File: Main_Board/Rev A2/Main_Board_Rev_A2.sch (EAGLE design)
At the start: 209 parts, among them J1 90814-0208, J12 22-27-2061-06, J15 1241050-5, J2 90814-0206, J3 90814-0208, J4 5504F1-09S-02A-03, J5 22-05-7048-04, J6 22-05-7048-04, J7 22-05-7058-05, J8 22-05-7048-04, J9 22-05-7028-02, K1 G6K-2G-Y, K2 G6K-2G-Y, K3 G6K-2G-Y, K4 G6K-2G-Y, P1 RB1-125BAG1A, SW1 B3FS-1050, SW2 B3FS-1050, T2 MMBT2222AL, U1 LT3686HDDPBF, U10 SN74LVC2G17DBVR, U11 MCP2561-E/SN, U12 TLV313, U2 TPL0401A, U3 SN74LVC3G17DCTR, U4 SN74LVC3G17DCTR, U5 LT3686HDDPBF, U6 LPC1768FBD100, U7 AT24C512C-SSHM-B, U8 SN74LVC3G17DCTR, U9 SN74LVC2G17DBVR, X1 ASE_50, X12 22-05-7038-03, X13 22-05-7038-03, X14 22-05-7038-03, X15 22-05-7038-03, X2 FC-135, X3 ASE-12, X4 MSTBA2, X5 22-05-7028-02, X6 USB3075-30-A, X7 3000, X8 22-05-7028-02

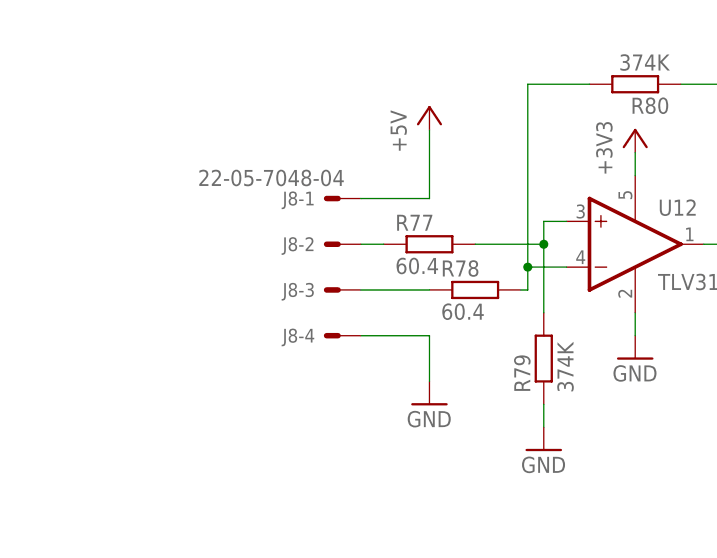
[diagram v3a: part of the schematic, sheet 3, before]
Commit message: Replace load pin connector into 5pts molex connector with GND MECA
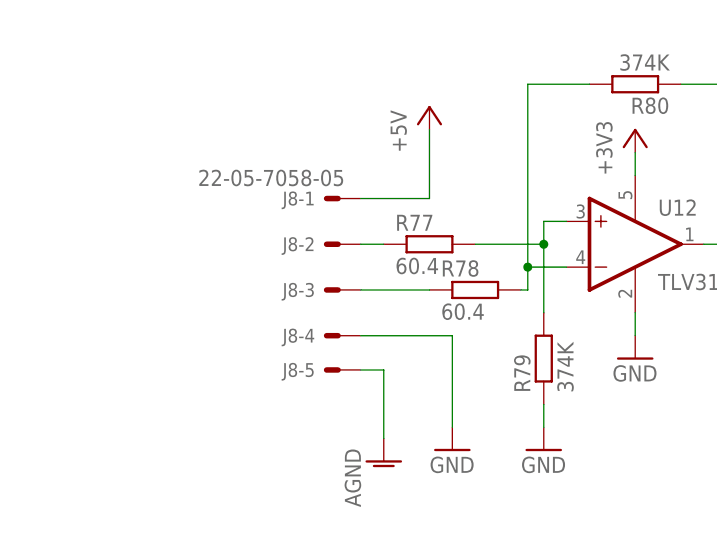
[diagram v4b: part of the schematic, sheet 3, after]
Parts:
- J8: value 22-05-7048-04 -> 22-05-7058-05; device con-molex:22-05-7048-04 -> con-molex:22-05-7058-05
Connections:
- net AGND: now also J8-5.S
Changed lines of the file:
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@@
 <attribute name="OC_NEWARK" value="86T3649"/>
 </part>
-<part name="J8" library="con-molex" deviceset="22-?-04" device="05-7048">
+<part name="J8" library="con-molex" deviceset="22-?-05" device="05-7058">
 <attribute name="MPN" value="22-05-7048"/>
 <attribute name="OC_NEWARK" value="26M6363"/>
@@
 <part name="GND88" library="supply1" deviceset="GND" device=""/>
 <part name="GND99" library="supply1" deviceset="GND" device=""/>
+<part name="AGND5" library="supply1" deviceset="AGND" device=""/>
 </parts>
 <sheets>
@@
 <instance part="J8" gate="-4" x="40.64" y="26.67" rot="MR0"/>
 <instance part="P+21" gate="1" x="50.8" y="52.07"/>
-<instance part="GND94" gate="1" x="50.8" y="19.05"/>
+<instance part="GND94" gate="1" x="53.34" y="13.97"/>
 <instance part="U12" gate="G$1" x="73.66" y="36.83">
 <attribute name="OC_NEWARK" x="73.66" y="36.83" size="1.778" layer="96" display="off"/>
@@
 <instance part="X12" gate="-3" x="40.64" y="137.16" rot="R180"/>
 <instance part="GND99" gate="1" x="45.72" y="124.46"/>
+<instance part="J8" gate="-5" x="40.64" y="22.86" rot="R180"/>
+<instance part="AGND5" gate="VR1" x="45.72" y="12.7"/>
 </instances>
 <busses>
@@
 <pinref part="J8" gate="-4" pin="S"/>
 <pinref part="GND94" gate="1" pin="GND"/>
-<wire x1="43.18" y1="26.67" x2="50.8" y2="26.67" width="0.1524" layer="91"/>
-<wire x1="50.8" y1="26.67" x2="50.8" y2="21.59" width="0.1524" layer="91"/>
+<wire x1="43.18" y1="26.67" x2="53.34" y2="26.67" width="0.1524" layer="91"/>
+<wire x1="53.34" y1="26.67" x2="53.34" y2="16.51" width="0.1524" layer="91"/>
 </segment>
 <segment>
@@
 </segment>
 </net>
+<net name="AGND" class="0">
+<segment>
+<pinref part="AGND5" gate="VR1" pin="AGND"/>
+<pinref part="J8" gate="-5" pin="S"/>
+<wire x1="45.72" y1="15.24" x2="45.72" y2="22.86" width="0.1524" layer="91"/>
+<wire x1="45.72" y1="22.86" x2="43.18" y2="22.86" width="0.1524" layer="91"/>
+</segment>
+</net>

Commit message: Generate MDP files
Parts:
- removed C102, C105, C129, C130, C131, C132, C133, C134: 0.1uF, rcl:C-EUC0603
- removed D3: MBRS140, diode:MBRS140
- removed GND: DP83848JSQ/NOPB, textas:DP83848JSQ/NOPB
- removed JP5: FIDUCIAL1X2, SparkFun:FIDUCIAL1X2
- removed P1: RB1-125BAG1A, con-wiznet:RB1-125BAG1A
- removed R108, R109, R110, R111: 100, rcl:R-EU_R0603
- removed X12, X13, X14, X15: 22-05-7038-03, con-molex:22-05-7038-03
- removed X7: 3000, keystone:3000
- removed X8: 22-05-7028-02, con-molex:22-05-7028-02
- added C46, C47, C50, C51: 2.2uF, rcl:C-EUC0603
- added C48, C49: 1000pF, rcl:C-EUC0603
- added C52, C53: 22uF, rcl:C-EUC0805
- added D1: MBRS140, diode:MBRS140
- added J10: 22-05-7048-04, con-molex:22-05-7048-04
- added J11: 22-05-7058-05, con-molex:22-05-7058-05
- added J14: 90814-0208, Molex_By_element14_Batch_1:90814-0208
- added J16: 90814-0206, Molex_By_element14_Batch_1:90814-0206
- added J17: MSTBA2, con-phoenix-508:MSTBA2
- added J18: 22-27-2061-06, con-molex:22-27-2061-06
- added J20: 1241050-5, con-amp:1241050-5
- added JP3: FIDUCIAL1X2, SparkFun:FIDUCIAL1X2
- added R15: 0R, rcl:R-EU_R0603
- added R60: 1K, rcl:R-EU_R0603
- added R66: 100, rcl:R-EU_R0603
- added R81: 1K5, rcl:R-EU_R0603
- added U13: LT3686HDDPBF, lineartechnology:LT3686HDDPBF
- C1: value 2.2uF -> 4.7uF; device rcl:C-EUC0603 -> rcl:CPOL-EUCT3216; MPN GRT188R61H225KE13D -> F931A475MAA; OC_NEWARK 01AC8938 -> 58R3271
- C10, C11: value 4.7uF -> 100nF; MPN MC0603X475K100CT -> MC0603B104K250CT; OC_NEWARK 06X6198 -> 06R4925
- C12: value 22uF -> 100nF; device rcl:C-EUC0805 -> rcl:C-EUC0603; MPN (none) -> MC0603B104K250CT; OC_NEWARK unknown -> 06R4925
- C16, C18, C20, C21, C22: value 100nF -> 0.1uF; MPN MC0603B104K250CT -> MC0603B104K160CT; OC_NEWARK 06R4925 -> 06R4923
- C17: value 10uF -> 0.1uF; device rcl:CPOL-EUCT3216 -> rcl:C-EUC0603; MPN F931A106MAA -> MC0603B104K160CT; OC_NEWARK 58R3260 -> 06R4923
- C19: value 100nF -> 18pF; MPN MC0603B104K250CT -> MC0603N180K500CT; OC_NEWARK 06R4925 -> 06R5140
- C2, C6: value 2.2uF -> 100nF; MPN GRT188R61H225KE13D -> MC0603B104K250CT; OC_NEWARK 01AC8938 -> 06R4925
- C23: value 4700pF -> 0.1uF; MPN MC0603B472K500CT -> MC0603B104K160CT; OC_NEWARK 33R0458 -> 06R4923
- C24: value 22uF -> 18pF; device rcl:C-EUC0805 -> rcl:C-EUC0603; MPN (none) -> MC0603N180K500CT; OC_NEWARK unknown -> 06R5140
- C26, C27: value 18pF -> 0.1uF; MPN MC0603N180K500CT -> MC0603B104K160CT; OC_NEWARK 06R5140 -> 06R4923
- C3: value 1000pF -> 100nF; MPN MC0603B102K500CT -> MC0603B104K250CT; OC_NEWARK 06R4910 -> 06R4925
- C35: value 10uF -> 4.7uF; device rcl:CPOL-EUCT3216 -> rcl:C-EUC0603; MPN F931A106MAA -> MC0603X475K100CT; OC_NEWARK 58R3260 -> 06X6198
- C36: value 0.1uF -> 4.7uF; MPN MC0603B104K160CT -> MC0603X475K100CT; OC_NEWARK 06R4923 -> 06X6198
- C4: value 1000pF -> 10uF; device rcl:C-EUC0603 -> rcl:CPOL-EUCT3216; MPN MC0603B102K500CT -> F931A106MAA; OC_NEWARK 06R4910 -> 58R3260
- C5: value 2.2uF -> 4700pF; MPN GRT188R61H225KE13D -> MC0603B472K500CT; OC_NEWARK 01AC8938 -> 33R0458
- C9: value 4.7uF -> 10uF; MPN F931A475MAA -> F931A106MAA; OC_NEWARK 58R3271 -> 58R3260
- J1: value 90814-0208 -> 22-05-7028-02; device Molex_By_element14_Batch_1:90814-0208 -> con-molex:22-05-7028-02
- J12: value 22-27-2061-06 -> 22-05-7028-02; device con-molex:22-27-2061-06 -> con-molex:22-05-7028-02; MF MOLEX -> (none); MPN 22-27-2061 -> 22-05-7028; OC_NEWARK 56H0719 -> 25M1728
- J15: value 1241050-5 -> 90814-0208; device con-amp:1241050-5 -> Molex_By_element14_Batch_1:90814-0208; MPN 1241050-5 -> (none); OC_NEWARK 98K5467 -> (none)
- J2: value 90814-0206 -> RB1-125BAG1A; device Molex_By_element14_Batch_1:90814-0206 -> con-wiznet:RB1-125BAG1A; OC_NEWARK (none) -> unknown
- J3: value 90814-0208 -> 5504F1-09S-02A-03; device Molex_By_element14_Batch_1:90814-0208 -> con-multicomp:5504F1-09S-02A-03; MPN (none) -> 5504F1-09S-02A-03; OC_NEWARK (none) -> 18T0703
- J4: value 5504F1-09S-02A-03 -> 22-05-7038-03; device con-multicomp:5504F1-09S-02A-03 -> con-molex:22-05-7038-03; MPN 5504F1-09S-02A-03 -> 22-05-7038; OC_NEWARK 18T0703 -> 26M6362
- J5: value 22-05-7048-04 -> 22-05-7038-03; device con-molex:22-05-7048-04 -> con-molex:22-05-7038-03; MPN 22-05-7048 -> 22-05-7038; OC_NEWARK 26M6363 -> 26M6362
- J6: value 22-05-7048-04 -> 22-05-7038-03; device con-molex:22-05-7048-04 -> con-molex:22-05-7038-03; MPN 22-05-7048 -> 22-05-7028; OC_NEWARK 26M6363 -> 25M1728
- J7: value 22-05-7058-05 -> 22-05-7038-03; device con-molex:22-05-7058-05 -> con-molex:22-05-7038-03; MF MOLEX -> (none); MPN 22-05-7058 -> 22-05-7028; OC_NEWARK 55H9619 -> 25M1728
- J9: value 22-05-7028-02 -> 22-05-7048-04; device con-molex:22-05-7028-02 -> con-molex:22-05-7048-04; MPN (none) -> 22-05-7048; OC_NEWARK (none) -> 26M6363
- L1: value 10uH -> 0603PS-103KLB; device Wurth-POWER_MAGNETICS-rev16f:WE-PD2_5848/5820 -> coilcraft:0603PS; MPN 74477410 -> (none); OC_NEWARK 08P2817 -> unknown
- L3: value 0603PS-103KLB -> 10uH; device coilcraft:0603PS -> Wurth-POWER_MAGNETICS-rev16f:WE-PD2_5848/5820; MPN (none) -> 74477410; OC_NEWARK unknown -> 08P2817
- LED1: value Red -> Blue; MPN OVS-0608 -> OVS-0603; OC_NEWARK 15R2208 -> 15R2205
- LED6: value Blue -> Red; MPN OVS-0603 -> OVS-0608; OC_NEWARK 15R2205 -> 15R2208
- R1: value 1K5 -> 220; MPN MCMR06X1501FTL -> MCMR06X2200FTL; OC_FARNELL 2073391 -> (none); OC_NEWARK 86T3542 -> 86T3577
- R10: value 1K -> 2K2; MPN MCMR06X1001FTL -> MCMR06X2201FTL; OC_NEWARK 86T3505 -> 86T3578
- R11: value 1K -> 10K; MPN MCMR06X1001FTL -> MCMR06X4701FTL; OC_NEWARK 86T3505 -> 86T3649
- R12, R13, R58, R9: value 1K -> 4K7; MPN MCMR06X1001FTL -> MCMR06X4701FTL; OC_NEWARK 86T3505 -> 86T3649
- R14: value 4K7 -> 0R; MPN MCMR06X4701FTL -> MCMR06X000 PTL; OC_NEWARK 86T3649 -> 86T3500
- R16: value 1K5 -> 10K; MPN MCMR06X1501FTL -> MCMR06X1002FTL; OC_FARNELL 2073391 -> (none); OC_NEWARK 86T3542 -> 86T3506
- R17: value 4K7 -> 10K; MPN MCMR06X4701FTL -> MCMR06X1002FTL; OC_NEWARK 86T3649 -> 86T3506
- R18, R19: value 220 -> 0R; MPN MCMR06X2200FTL -> MCMR06X000 PTL; OC_NEWARK 86T3577 -> 86T3500
- R2: value 4K7 -> 220; MPN MCMR06X4701FTL -> MCMR06X2200FTL; OC_NEWARK 86T3649 -> 86T3577
- R20: value 49.9 -> 1K5; MPN MCMR06X49R9FTL -> MCMR06X1501FTL; OC_NEWARK 86T3659 -> 86T3542
- R21, R22, R23: value 49.9 -> 100; MPN MCMR06X49R9FTL -> MCMR06X1000FTL; OC_NEWARK 86T3659 -> 86T3504
- R24: value 4K7 -> 100; MPN MCMR06X4701FTL -> MCMR06X1000FTL; OC_NEWARK 86T3649 -> 86T3504
- R25, R26: value 4K7 -> 60.4; MPN MCMR06X4701FTL -> MCMR06X1801FTL; OC_NEWARK 86T3649 -> 86T3556
- R27: value 4K7 -> 374K; MPN MCMR06X4701FTL -> MCMR06X1201FTL; OC_NEWARK 86T3649 -> 86T3525
- R28: value 2K2 -> 4K7; MPN MCMR06X2201FTL -> MCMR06X4701FTL; OC_NEWARK 86T3578 -> 86T3649
- R29: value 31K6 -> 4K7; MPN MC0603SAF3162T5E -> MCMR06X4701FTL; OC_FARNELL 2073391 -> (none); OC_NEWARK 79M5962 -> 86T3649
- R3: value 1K5 -> 49.9; MPN MCMR06X1501FTL -> MCMR06X49R9FTL; OC_NEWARK 86T3542 -> 86T3659
- R30: value 31K6 -> 374K; MPN MC0603SAF3162T5E -> MCMR06X1201FTL; OC_FARNELL 2073391 -> (none); OC_NEWARK 79M5962 -> 86T3525
- R31: value 10K -> 4K7; MPN MCMR06X1002FTL -> MCMR06X4701FTL; OC_FARNELL 2073391 -> (none); OC_NEWARK 86T3506 -> 86T3649
- R32: value 10K -> 4K7; MPN MCMR06X1002FTL -> MCMR06X4701FTL; OC_NEWARK 86T3506 -> 86T3649
- R33: value 52K3 -> 100; MPN MC0063W0603152K3 -> MCMR06X1000FTL; OC_FARNELL 2073391 -> (none); OC_NEWARK 26M0962 -> 86T3504
- R34, R37, R40: value 10K -> 100; MPN MCMR06X1002FTL -> MCMR06X1000FTL; OC_NEWARK 86T3506 -> 86T3504
- R35, R36: value 33 -> 1K5; MPN MCMR06X33R0FTL -> MCMR06X1501FTL; OC_NEWARK 86T3614 -> 86T3542
- R4, R5, R6: value 100 -> 49.9; MPN MCMR06X1000FTL -> MCMR06X49R9FTL; OC_NEWARK 86T3504 -> 86T3659
- R41, R47, R62: value 100 -> 1K; MPN MCMR06X1000FTL -> MCMR06X1001FTL; OC_NEWARK 86T3504 -> 86T3505
- R42, R46, R48: value 4K7 -> 1K; MPN MCMR06X4701FTL -> MCMR06X1001FTL; OC_NEWARK 86T3649 -> 86T3505
- R43, R45: value 100 -> 2K7; MPN MCMR06X1000FTL -> MCMR06X4701FTL; OC_NEWARK 86T3504 -> 86T3649
- R44: value 4K7 -> 2K7
- R49: OC_FARNELL 2073391 -> (none)
- R50, R51, R52: value 1K5 -> 10K; MPN MCMR06X1501FTL -> MCMR06X1002FTL; OC_NEWARK 86T3542 -> 86T3506
- R53: value 1K5 -> 100; MPN MCMR06X1501FTL -> MCMR06X1000FTL; OC_NEWARK 86T3542 -> 86T3504
- R54, R55: value 60.4 -> 100; MPN MCMR06X60R4FTL -> MCMR06X1000FTL; OC_NEWARK 86T3680 -> 86T3504
- R56: value 31K6 -> 100; MPN MC0603SAF3162T5E -> MCMR06X1000FTL; OC_FARNELL 2073391 -> (none); OC_NEWARK 79M5962 -> 86T3504
- R57: value 10K -> 4K7
- R61: value 100 -> 1K; MPN MCMR06X33R0FTL -> MCMR06X1001FTL; OC_NEWARK 86T3614 -> 86T3505
- R63, R64: value 10K -> 1K; MPN MCMR06X1002FTL -> MCMR06X1001FTL; OC_NEWARK 86T3506 -> 86T3505
- R65: value 0R -> 100; MPN MCMR06X000 PTL -> MCMR06X33R0FTL; OC_NEWARK 86T3500 -> 86T3614
- R67, R68: value 0R -> 31K6; MPN MCMR06X000 PTL -> MC0603SAF3162T5E; OC_FARNELL (none) -> 2073391; OC_NEWARK 86T3500 -> 79M5962
- R69: value 0R -> 4K7; MPN MCMR06X000 PTL -> MCMR06X4701FTL; OC_NEWARK 86T3500 -> 86T3649
- R7: value 100 -> 60.4; MPN MCMR06X1000FTL -> MCMR06X60R4FTL; OC_NEWARK 86T3504 -> 86T3680
- R70: value 1K5 -> 4K7; MPN MCMR06X1501FTL -> MCMR06X4701FTL; OC_NEWARK 86T3542 -> 86T3649
- R71: value 2K7 -> 52K3; MPN MCMR06X4701FTL -> MC0063W0603152K3; OC_FARNELL (none) -> 2073391; OC_NEWARK 86T3649 -> 26M0962
- R72, R74: value 1K -> 10K; MPN MCMR06X1001FTL -> MCMR06X1002FTL; OC_FARNELL (none) -> 2073391; OC_NEWARK 86T3505 -> 86T3506
- R73: value 2K7 -> 31K6; MPN MCMR06X4701FTL -> MC0603SAF3162T5E; OC_FARNELL (none) -> 2073391; OC_NEWARK 86T3649 -> 79M5962
- R75: value 1K -> 1K5; MPN MCMR06X1001FTL -> MCMR06X1501FTL; OC_FARNELL (none) -> 2073391; OC_NEWARK 86T3505 -> 86T3542
- R76: value 2K7 -> 1K5; MPN MCMR06X4701FTL -> MCMR06X1501FTL; OC_FARNELL (none) -> 2073391; OC_NEWARK 86T3649 -> 86T3542
- R77: value 60.4 -> 1K5; MPN MCMR06X1801FTL -> MCMR06X1501FTL; OC_NEWARK 86T3556 -> 86T3542
- R78: value 60.4 -> 33; MPN MCMR06X1801FTL -> MCMR06X33R0FTL; OC_NEWARK 86T3556 -> 86T3614
- R79: value 374K -> 33; MPN MCMR06X1201FTL -> MCMR06X33R0FTL; OC_NEWARK 86T3525 -> 86T3614
- R8: value 1K -> 60.4; MPN MCMR06X1001FTL -> MCMR06X60R4FTL; OC_NEWARK 86T3505 -> 86T3680
- R80: value 374K -> 1K5; MPN MCMR06X1201FTL -> MCMR06X1501FTL; OC_NEWARK 86T3525 -> 86T3542
- U1: value LT3686HDDPBF -> DP83848JSQ/NOPB; device lineartechnology:LT3686HDDPBF -> textas:DP83848JSQ/NOPB; MPN (none) -> DP83848JSQ/NOPB; OC_NEWARK (none) -> 96W2841
- U10, U9: value SN74LVC2G17DBVR -> SN74LVC3G17DCTR; device ti:SN74LVC2G17DBVR -> ti:SN74LVC3G17DCTR
- U11: value MCP2561-E/SN -> TPL0401A; device Microchip_By_element14_Batch_1:MCP2561-E/SN -> ti:TPL0401A; MPN MCP2561-E/SN -> ISL90727WIE627Z-T7A; OC_NEWARK 12X8698 -> 82Y6761
- U12: value TLV313 -> LT3686HDDPBF; device ti:TLV313 -> lineartechnology:LT3686HDDPBF; MPN TLV313IDBVT -> (none); OC_NEWARK 95Y0395 -> (none)
- U2: value TPL0401A -> MCP2561-E/SN; device ti:TPL0401A -> Microchip_By_element14_Batch_1:MCP2561-E/SN; MPN ISL90727WIE627Z-T7A -> MCP2561-E/SN; OC_NEWARK 82Y6761 -> 12X8698
- U3: value SN74LVC3G17DCTR -> AT24C512C-SSHM-B; device ti:SN74LVC3G17DCTR -> atmel:AT24C512C-SSHM-B; MF TEXAS INSTRUMENTS -> (none)
- U4: value SN74LVC3G17DCTR -> LPC1768FBD100; device ti:SN74LVC3G17DCTR -> NXP:LPC1768FBD100; MF TEXAS INSTRUMENTS -> (none); MPN (none) -> LPC1768FBD100; OC_NEWARK (none) -> 15R1840
- U5: value LT3686HDDPBF -> TLV313; device lineartechnology:LT3686HDDPBF -> ti:TLV313; MPN (none) -> TLV313IDBVT; OC_NEWARK (none) -> 95Y0395
- U6: value LPC1768FBD100 -> SN74LVC2G17DBVR; device NXP:LPC1768FBD100 -> ti:SN74LVC2G17DBVR; MF (none) -> TEXAS INSTRUMENTS; MPN LPC1768FBD100 -> (none); OC_NEWARK 15R1840 -> (none)
- U7: value AT24C512C-SSHM-B -> SN74LVC2G17DBVR; device atmel:AT24C512C-SSHM-B -> ti:SN74LVC2G17DBVR; MF (none) -> TEXAS INSTRUMENTS
- X4: value MSTBA2 -> 3000; device con-phoenix-508:MSTBA2 -> keystone:3000; MF (none) -> KEYSTONE ELECTR; MPN (none) -> 3000; OC_NEWARK (none) -> 66F5622
- renumbered C101 to C43, C103 to C39, C104 to C41, C106 to C40, C107 to C42, C108 to C44, C109 to C45, U$2 to T1, X5 to J13, X6 to J19
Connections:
- net !JTAG_TRST: now also J20.P$5, U4.*TRST; no longer J15.P$5, U6.*TRST
- net !RESET: now also R14.1, R16.1, U4.*RESET; no longer R63.1, R65.1, U6.*RESET
- net +24V: now also C46.1, C47.1, J10-1.S, J3C.9, J4-1.S, J7-1.S, J9-1.S, R69.2, R70.2, U12.EN/UVLO, U12.VIN, U13.EN/UVLO, U13.VIN; no longer C1.1, C2.1, J4C.9, R25.2, R26.2, U1.EN/UVLO, U1.VIN, U5.EN/UVLO, U5.VIN, X12-1.S, X13-1.S, X14-1.S, X15-1.S
- net +3V3: now also C1.+, C10.1, C11.1, C13.1, C16.1, C17.1, C2.1, C20.1, C21.1, C26.1, C27.1, C3.1, C53.1, J15.1, J16.1, J2.CT, J20.P$1, L1.1, L3.2, LED1.A, R10.1, R11.2, R12.2, R13.2, R16.2, R2.2, R4.1, R5.1, R57.1, R58.1, R6.1, R73.2, R76.2, R80.1, R81.1, U1.AVDD33, U1.IOVDD33, U1.IOVDD33_2, U13.BD, U4.NC, U4.VDD, U4.VDD_2, U4.VDD_3, U4.VDD_4, U4.VDD_5, U4.VDD_6, U5.V+, U6.VCC; no longer C129.1, C130.1, C14.1, C19.1, C29.1, C30.1, C31.1, C35.+, C36.1, C37.1, C38.1, C7.1, C8.1, GND.AVDD33, GND.IOVDD33, GND.IOVDD33_2, J15.P$1, J2.1, J3.1, L1.2, L3.1, LED5.A, P1.CT, R14.1, R18.2, R19.2, R2.1, R20.1, R21.1, R22.1, R23.1, R27.2, R28.1, R38.1, R56.2, R57.2, R63.2, R64.2, U1.BD, U12.V+, U4.VCC, U6.NC, U6.VDD, U6.VDD_2, U6.VDD_3, U6.VDD_4, U6.VDD_5, U6.VDD_6
- net +5V: now also C14.1, C52.1, J1-1.S, J11-4.S, J14.4, R28.1, R29.1, R31.1, R32.1, R35.2, R36.2, R38.2, R39.2, R43.1, R45.1, R65.1, R71.2, R75.2, U11.H, U12.BD; no longer C13.1, C24.1, J1.4, J7-4.S, J9-1.S, R16.2, R33.2, R42.1, R46.1, R48.1, R50.2, R51.2, R52.2, R53.2, R61.1, R71.1, R73.1, R76.1, U2.H, U5.BD
- net ADC_SLACK_DETECTION: now also R30.1, U4.P0[23]/AD0[0]/I2SRX_CLK/CAP3[0], U5.OUT; no longer R80.1, U12.OUT, U6.P0[23]/AD0[0]/I2SRX_CLK/CAP3[0]
- net ADC_TEMP_0: now also C35.1, R51.1, U4.P0[25]/AD0[2]/I2SRX_SDA/TXD3; no longer C11.1, R40.1, U6.P0[25]/AD0[2]/I2SRX_SDA/TXD3
- net ADC_TEMP_1: now also C36.1, R52.2, U4.P0[24]/AD0[1]/I2SRX_WS/CAP3[1]; no longer C10.1, R34.2, U6.P0[24]/AD0[1]/I2SRX_WS/CAP3[1]
- net AGND: now also J2.P$1, J3S.SHIELD; no longer J4S.SHIELD, P1.P$1
- net AVDD: now also C23.1, J12-1.S, L1.2, U4.VDDA, U4.VREFP; no longer C28.1, L3.2, U6.VDDA, U6.VREFP, X8-1.S
- net BOOT_SELECT_P2_10: now also R18.1, U4.P2[10]/*EINT0/NMI; no longer R68.1, U6.P2[10]/*EINT0/NMI
- net BOOT_SELECT_P2_12: now also R19.1, U4.P2[12]/*EINT2/I2STX_WS; no longer R69.1, U6.P2[12]/*EINT2/I2STX_WS
- net BRAKE_SENSOR_1: now also U4.P1[22]/MCOB0/USB_PWRD/MAT1[0], U6.1Y; no longer U10.1Y, U6.P1[22]/MCOB0/USB_PWRD/MAT1[0]
- net BRAKE_SENSOR_2: now also U4.P1[25]/MCOA1/MAT1[1], U6.2Y; no longer U10.2Y, U6.P1[25]/MCOA1/MAT1[1]
- net CAN_N: now also J3C.2, R7.1, U2.CANL; no longer J4C.2, R55.1, U11.CANL
- net CAN_P: now also J3C.7, R8.2, U2.CANH; no longer J4C.7, R54.2, U11.CANH
- net CAN_SHLD: now also J3C.5; no longer J4C.5
- net CAN_SPLIT: now also C5.2, U2.SPLIT; no longer C23.2, U11.SPLIT
- net CAN_X_N: now also U2.RXD, U4.P0[0]/RD1/TXD3/SDA1; no longer U11.RXD, U6.P0[0]/RD1/TXD3/SDA1
- net CAN_X_P: now also U2.TXD, U4.P0[1]/TD1/RXD3/SCL1; no longer U11.TXD, U6.P0[1]/TD1/RXD3/SCL1
- net DRIVE_EN: now also U4.P1[26]/MCOB1/PWM1[6]/CAP0[0], U7.1Y; no longer U6.P1[26]/MCOB1/PWM1[6]/CAP0[0], U9.1Y
- net DRIVE_ERR: now also U4.P1[29]/MCOB2/PCAP1[1]/MAT0[1], U7.2Y; no longer U6.P1[29]/MCOB2/PCAP1[1]/MAT0[1], U9.2Y
- net EEPROM_SCL: now also R13.1, U3.SCL, U4.P0[28]/SCL0/USB_SCL; no longer R27.1, U6.P0[28]/SCL0/USB_SCL, U7.SCL
- net EEPROM_SDA: now also R12.1, U3.SDA, U4.P0[27]/SDA0/USB_SDA; no longer R17.1, U6.P0[27]/SDA0/USB_SDA, U7.SDA
- net ENCODER_A: now also U4.P1[20]/MCI0/PWM1[2]/SCK0; no longer U6.P1[20]/MCI0/PWM1[2]/SCK0
- net ENCODER_B: now also U4.P1[23]/MCI1/PWM1[4]/MISO0; no longer U6.P1[23]/MCI1/PWM1[4]/MISO0
- net ENCODER_Z: now also U4.P1[24]/MCI2/PWM1[5]/MOSI0; no longer U6.P1[24]/MCI2/PWM1[5]/MOSI0
- net ETH_CLK_EN: now also U4.P1[27]/CLKOUT/*USB_OVRCR/CAP0[1]; no longer U6.P1[27]/CLKOUT/*USB_OVRCR/CAP0[1]
- net ETH_CRS: now also U1.CRS/CRS_DV/LED_CFG, U4.P1[8]/ENET_CRS; no longer GND.CRS/CRS_DV/LED_CFG, U6.P1[8]/ENET_CRS
- net ETH_MDC: now also U1.MDC, U4.P1[16]/ENET_MDC; no longer GND.MDC, U6.P1[16]/ENET_MDC
- net ETH_MDIO: now also U1.MDIO, U4.P1[17]/ENET_MDIO; no longer GND.MDIO, U6.P1[17]/ENET_MDIO
- net ETH_RST: now also U1.RESET_N, U4.P1[28]/MCOA2/PCAP1[0]/MAT0[0]; no longer GND.RESET_N, U6.P1[28]/MCOA2/PCAP1[0]/MAT0[0]
- net ETH_RXD_0: now also U1.RXD_0/PHYAD1, U4.P1[9]/ENET_RXD0; no longer GND.RXD_0/PHYAD1, U6.P1[9]/ENET_RXD0
- net ETH_RXD_1: now also U1.RXD_1/PHYAD2, U4.P1[10]/ENET_RXD1; no longer GND.RXD_1/PHYAD2, U6.P1[10]/ENET_RXD1
- net ETH_RX_ER: now also U1.RX_ER/MDIX_EN, U4.P1[14]/ENET_RX_ER; no longer GND.RX_ER/MDIX_EN, U6.P1[14]/ENET_RX_ER
- net ETH_RX_N: now also J2.RD-, R6.2, U1.RD-; no longer GND.RD-, P1.RD-, R23.2
- net ETH_RX_P: now also J2.RD+, R5.2, U1.RD+; no longer GND.RD+, P1.RD+, R22.2
- net ETH_TXD_0: now also U1.TXD_0, U4.P1[0]/ENET_TXD0; no longer GND.TXD_0, U6.P1[0]/ENET_TXD0
- net ETH_TXD_1: now also U1.TXD_1, U4.P1[1]/ENET_TXD1; no longer GND.TXD_1, U6.P1[1]/ENET_TXD1
- net ETH_TXD_EN: now also U1.TX_EN, U4.P1[4]/ENET_TX_EN; no longer GND.TX_EN, U6.P1[4]/ENET_TX_EN
- net ETH_TX_N: now also J2.TD-, R4.2, U1.TD-; no longer GND.TD-, P1.TD-, R21.2
- net ETH_TX_P: now also J2.TD+, R3.2, U1.TD+; no longer GND.TD+, P1.TD+, R20.2
- net ETH_X1: now also U1.X1, U4.P1[15]/ENET_REF_CLK; no longer GND.X1, U6.P1[15]/ENET_REF_CLK
- net FAN_1_PWM: now also R41.2, U4.P3[25]/MAT0[0]/PWM1[2]; no longer R58.2, U6.P3[25]/MAT0[0]/PWM1[2]
- net FAN_2_PWM: now also R42.2, U4.P3[26]/STCLK/MAT0[1]/PWM1[3]; no longer R59.2, U6.P3[26]/STCLK/MAT0[1]/PWM1[3]
- net GND: now also C1.-, C17.2, C23.2, C35.2, C4.-, C46.2, C47.2, C48.2, C49.2, C52.2, C53.2, C6.2, J1-2.S, J10-4.S, J11-1.S, J14.2, J14.3, J15.8, J16.6, J17-2.1, J18-1.S, J2.R4, J2.R5, J2.R6, J20.P$2, J3C.3, J3C.6, J4-3.S, J5-3.S, J6-3.S, J7-3.S, J9-4.S, LED7.C, LED8.C, LED9.C, R27.1, R50.2, R67.1, R68.1, R72.1, R74.1, R9.2, U1.AGND, U1.AGND_2, U1.DAP, U1.DGND, U1.IOGND, U11.GND, U12.EP, U12.MODE, U13.EP, U13.MODE, U2.STBY, U2.VSS, U3.A0, U3.A1, U3.A2, U4.VREFN, U4.VSS, U4.VSSA, U4.VSS_2, U4.VSS_3, U4.VSS_4, U4.VSS_5, U4.VSS_6, U5.V-, U6.GND, X4.VBAT-; no longer C1.2, C102.2, C105.2, C129.2, C130.2, C131.2, C132.2, C133.2, C134.2, C17.-, C35.-, C4.2, GND.AGND, GND.AGND_2, GND.DAP, GND.DGND, GND.IOGND, J1.2, J1.3, J12-1.S, J15.P$2, J2.6, J3.8, J4C.3, J4C.6, J5-4.S, J6-4.S, J7-1.S, J9-2.S, LED2.C, LED3.C, LED4.C, P1.R4, P1.R5, P1.R6, R24.2, R29.1, R30.1, R31.1, R32.2, R37.1, R79.1, U1.EP, U1.MODE, U11.STBY, U11.VSS, U12.V-, U2.GND, U4.GND, U5.EP, U5.MODE, U6.VREFN, U6.VSS, U6.VSSA, U6.VSS_2, U6.VSS_3, U6.VSS_4, U6.VSS_5, U6.VSS_6, U7.A0, U7.A1, U7.A2, X12-3.S, X13-3.S, X14-3.S, X15-3.S, X4-2.1, X7.VBAT-
- net HMI_BUTTON_1: now also J15.2, R59.1; no longer J3.2, R13.1
- net HMI_BUTTON_2: now also J15.3, R60.1; no longer J3.3, R12.1
- net HMI_BUTTON_3: now also J15.4, R61.1; no longer J3.4, R11.1
- net HMI_BUTTON_4: now also J15.5, R62.1; no longer J3.5, R10.1
- net HMI_BUTTON_5: now also J15.6, R63.1; no longer J3.6, R9.1
- net HMI_BUTTON_6: now also J15.7, R64.1; no longer J3.7, R8.1
- net HMI_BUTTON_ISO_1: now also U4.P0[16]/RXD1/SSEL0/SSEL, U9.1Y; no longer U4.1Y, U6.P0[16]/RXD1/SSEL0/SSEL
- net HMI_BUTTON_ISO_2: now also U4.P0[15]/TXD1/SCK0/SCK, U9.2Y; no longer U4.2Y, U6.P0[15]/TXD1/SCK0/SCK
- net HMI_BUTTON_ISO_3: now also U4.P0[17]/CTS1/MISO0/MISO, U9.3Y; no longer U4.3Y, U6.P0[17]/CTS1/MISO0/MISO
- net HMI_BUTTON_ISO_4: now also U10.1Y, U4.P0[18]/DCD1/MOSI0/MOSI; no longer U3.1Y, U6.P0[18]/DCD1/MOSI0/MOSI
- net HMI_BUTTON_ISO_5: now also U10.2Y, U4.P0[19]/DSR1/SDA1; no longer U3.2Y, U6.P0[19]/DSR1/SDA1
- net HMI_BUTTON_ISO_6: now also R14.2, R15.1, U10.3Y; no longer R65.2, R67.1, U3.3Y
- net HMI_BUTTON_MCU_FCT_6: now also R15.2, U4.P0[20]/DTR1/SCL1; no longer R67.2, U6.P0[20]/DTR1/SCL1
- net HMI_LCD_BACKLIGHT: now also R66.2, U4.P0[22]/RTS1/TD1; no longer R62.2, U6.P0[22]/RTS1/TD1
- net HMI_LCD_LED+: now also J14.1, R65.2; no longer J1.1, R61.2
- net HMI_LCD_SCL: now also J14.6, R57.2, U11.SCL, U4.P0[11]/RXD2/SCL2/MAT3[1]; no longer J1.6, R14.2, U2.SCL, U6.P0[11]/RXD2/SCL2/MAT3[1]
- net HMI_LCD_SDA: now also J14.5, R58.2, U11.SDA, U4.P0[10]/TXD2/SDA2/MAT3[0]; no longer J1.5, R2.2, U2.SDA, U6.P0[10]/TXD2/SDA2/MAT3[0]
- net HMI_LCD_VO: now also J14.7, U11.W; no longer J1.7, U2.W
- net HMI_LED_1: now also R55.1, U4.P2[2]/PWM1[3]/CTS1/TRACEDATA[3]; no longer R7.1, U6.P2[2]/PWM1[3]/CTS1/TRACEDATA[3]
- net HMI_LED_2: now also R53.2, U4.P2[3]/PWM1[4]/DCD1/TRACEDATA[2]; no longer R6.2, U6.P2[3]/PWM1[4]/DCD1/TRACEDATA[2]
- net HMI_LED_3: now also R56.1, U4.P2[4]/PWM1[5]/DSR1/TRACEDATA[1]; no longer R5.1, U6.P2[4]/PWM1[5]/DSR1/TRACEDATA[1]
- net HMI_LED_4: now also R54.2, U4.P2[5]/PWM1[6]/DTR1/TRACEDATA[0]; no longer R4.2, U6.P2[5]/PWM1[6]/DTR1/TRACEDATA[0]
- net ISP_RXDO: now also J18-4.S, J20.P$3, U4.P0[3]/RXD0/AD0[6]; no longer J12-4.S, J15.P$3, U6.P0[3]/RXD0/AD0[6]
- net ISP_TXDO: now also J18-5.S, J20.P$4, U4.P0[2]/TXD0/AD0[7]; no longer J12-5.S, J15.P$4, U6.P0[2]/TXD0/AD0[7]
- net JTAG_TCK: now also J20.P$8, U4.TCK/SWDCLK; no longer J15.P$8, U6.TCK/SWDCLK
- net JTAG_TDI: now also J20.P$7, U4.TDI; no longer J15.P$7, U6.TDI
- net JTAG_TDO: now also J20.P$9, U4.TDO/SWO; no longer J15.P$9, U6.TDO/SWO
- net JTAG_TMS: now also J20.P$10, U4.TMS/SWDIO; no longer J15.P$10, U6.TMS/SWDIO
- net L1_1: now also J2.L2, U1.LED_LINK/AN0; no longer GND.LED_LINK/AN0, P1.L2
- net L1_2: now also J2.L4, U1.LED_SPEED/AN1; no longer GND.LED_SPEED/AN1, P1.L4
- net LED_DEBUG: now also R20.2, U4.P0[9]/I2STX_SDA/MOSI1/MAT2[3]; no longer R70.2, U6.P0[9]/I2STX_SDA/MOSI1/MAT2[3]
- net MII_MODE: now also R10.2, U1.RX_DV/MII_MODE; no longer GND.RX_DV/MII_MODE, R28.2
- net N$1: now also J16.3, R53.1; no longer J2.3, R6.1
- net N$10: now also R68.2, U13.RT; no longer R30.2, U1.RT
- net N$11: now also J9-2.S, R41.1; no longer J5-2.S, R58.1
- net N$12: now also J11-3.S, R43.2, R46.1; no longer J7-3.S, R71.2, R72.1
- net N$13: now also J10-2.S, R42.1; no longer J6-2.S, R59.1
- net N$14: now also J11-5.S, R44.2, R47.1; no longer J7-5.S, R74.1, R76.2
- net N$15: now also R78.1, R81.2; no longer R3.2, R36.1
- net N$16: now also R79.1, R80.2; no longer R35.1, R38.2
- net N$17: now also C37.1, R59.2, U9.1A; no longer C102.1, R13.2, U4.1A
- net N$18: now also LED10.C, R77.1; no longer LED5.C, R39.1
- net N$19: now also R60.2, U9.2A; no longer R12.2, U4.2A
- net N$2: now also J16.5, R54.1; no longer J2.5, R4.1
- net N$20: now also R61.2, U9.3A; no longer R11.2, U4.3A
- net N$21: now also J4-2.S, R21.1; no longer R109.1, X14-2.S
- net N$22: now also C49.1, U13.SS; no longer C4.1, U1.SS
- net N$23: now also J5-2.S, R22.1; no longer R108.1, X15-2.S
- net N$24: now also K11.+, R21.2; no longer K31.+, R109.2
- net N$25: now also C38.1, R62.2, U10.1A; no longer C105.1, R10.2, U3.1A
- net N$26: now also R63.2, U10.2A; no longer R9.2, U3.2A
- net N$27: now also R64.2, U10.3A; no longer R8.2, U3.3A
- net N$28: now also K31.+, R23.2; no longer K11.+, R111.2
- net N$3: now also C5.1, R7.2, R8.1; no longer C23.1, R54.1, R55.2
- net N$30: now also R71.1, R72.2, U12.FB; no longer R31.2, R33.1, U5.FB
- net N$31: now also C50.1, U12.BOOST; no longer C5.1, U5.BOOST
- net N$32: now also J6-2.S, R23.1; no longer R111.1, X12-2.S
- net N$33: now also K41.+, R24.2; no longer K21.+, R110.2
- net N$34: now also C50.2, D1.C, U12.SW; no longer C5.2, D2.C, U5.SW
- net N$35: now also D1.A, U12.DA; no longer D2.A, U5.DA
- net N$36: now also R73.1, R74.2, U13.FB; no longer R49.2, R56.1, U1.FB
- net N$37: now also J7-2.S, R24.1; no longer R110.1, X13-2.S
- net N$38: now also C29.1, R34.2, U6.2A; no longer C131.1, R47.2, U10.2A
- net N$39: now also C28.1, R33.2, U6.1A; no longer C132.1, R45.2, U10.1A
- net N$4: now also R9.1, U1.RBIAS; no longer GND.RBIAS, R24.1
- net N$40: now also C51.1, U13.BOOST; no longer C6.1, U1.BOOST
- net N$41: now also C30.1, R37.2, U7.1A; no longer C134.1, R41.2, U9.1A
- net N$42: now also C31.1, R40.2, U7.2A; no longer C133.1, R43.2, U9.2A
- net N$43: now also C51.2, D2.C, L3.1, U13.SW; no longer C6.2, D3.C, L1.1, U1.SW
- net N$44: now also LED7.A, R70.1; no longer LED2.A, R26.1
- net N$45: now also LED6.C, R69.1; no longer LED1.C, R25.1
- net N$46: now also D2.A, U13.DA; no longer D3.A, U1.DA
- net N$47: now also R11.1, U3.WP; no longer R57.1, U7.WP
- net N$48: now also R17.1, R18.2, R19.2; no longer R64.1, R68.2, R69.2
- net N$49: now also LED1.C, R20.1; no longer LED10.C, R70.1
- net N$5: now also R67.2, U12.RT; no longer R29.2, U5.RT
- net N$50: now also LED9.A, R76.1; no longer LED4.A, R1.1
- net N$51: now also LED8.A, R75.1; no longer LED3.A, R16.1
- net N$52: now also J11-2.S, R45.2, R48.1; no longer J7-2.S, R73.2, R75.1
- net N$53: now also R48.2; no longer R75.2
- net N$54: now also R47.2; no longer R74.2
- net N$55: now also K21.+, R22.2; no longer K41.+, R108.2
- net N$58: now also K13.S, LED2.C, R28.2, R33.1; no longer K33.S, LED8.C, R45.1, R46.2
- net N$6: now also C48.1, U12.SS; no longer C3.1, U5.SS
- net N$61: now also R46.2; no longer R72.2
- net N$62: now also R25.1; no longer R77.1
- net N$63: now also J16.2, R55.2; no longer J2.2, R7.2
- net N$64: now also J16.4, R56.2; no longer J2.4, R5.2
- net N$65: now also J12-2.S, R49.2, R51.2; no longer R37.2, R40.2, X8-2.S
- net N$66: now also R50.1, R52.1; no longer R32.1, R34.1
- net N$67: now also R66.1; no longer R62.1
- net N$70: now also LED2.A, R35.1; no longer LED8.A, R52.1
- net N$71: now also K23.S, LED3.C, R29.2, R34.1; no longer K43.S, LED9.C, R47.1, R48.2
- net N$72: now also LED3.A, R36.1; no longer LED9.A, R53.1
- net N$73: now also K33.S, LED4.C, R31.2, R37.1; no longer K13.S, LED6.C, R41.1, R42.2
- net N$74: now also LED4.A, R38.1; no longer LED6.A, R50.1
- net N$75: now also K43.S, LED5.C, R32.2, R40.1; no longer K23.S, LED7.C, R43.1, R44.2
- net N$76: now also LED5.A, R39.1; no longer LED7.A, R51.1
- net N$78: now also R26.1; no longer R78.1
- net N$79: now also R25.2, R27.2, U5.+IN; no longer R77.2, R79.2, U12.+IN
- net N$8: now also J2.L1, R1.1; no longer P1.L1, R19.1
- net N$80: now also R26.2, R30.2, U5.-IN; no longer R78.2, R80.2, U12.-IN
- net N$9: now also J2.L3, R2.1; no longer P1.L3, R18.1
- net PFBOUT: now also C4.+, C6.1, C7.1, C8.1, U1.PFBIN1, U1.PFBIN2, U1.PFBOUT; no longer C16.1, C17.+, C20.1, C21.1, GND.PFBIN1, GND.PFBIN2, GND.PFBOUT
- net RTCX1: now also C19.1, U4.RTCX1; no longer C26.1, U6.RTCX1
- net RTCX2: now also C24.1, U4.RTCX2; no longer C27.1, U6.RTCX2
- net USB_D_N: now also R78.2, U4.P0[30]/USB_D?; no longer R36.2, U6.P0[30]/USB_D?
- net USB_D_P: now also R79.2, U4.P0[29]/USB_D+; no longer R35.2, U6.P0[29]/USB_D+
- net USB_UP_LED: now also R77.2, U4.P1[18]/USB_UP_LED/PWM1[1]/CAP1[0]; no longer R39.2, U6.P1[18]/USB_UP_LED/PWM1[1]/CAP1[0]
- net USB_V_BUS: now also U4.P1[30]/VBUS/AD0[4]; no longer U6.P1[30]/VBUS/AD0[4]
- net VBAT+: now also U4.VBAT, X4.VBAT+; no longer U6.VBAT, X7.VBAT+
- net VIN: now also J17-1.1, LED6.A; no longer LED1.A, X4-1.1
- net XTAL1: now also U4.XTAL1; no longer U6.XTAL1

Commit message: Update component reference
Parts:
- J1: MPN (none) -> 22-05-7028; OC_NEWARK (none) -> 25M1728
- J6, J7: MPN 22-05-7028 -> 22-05-7038; OC_NEWARK 25M1728 -> 26M6362
- J8: MF (none) -> MOLEX; MPN 22-05-7048 -> 22-05-7058; OC_NEWARK 26M6363 -> 55H9619
- R11: MPN MCMR06X4701FTL -> MCMR06X1002FTL; OC_NEWARK 86T3649 -> 86T3506
- R25, R26: MPN MCMR06X1801FTL -> MCMR06X60R4FTL; OC_NEWARK 86T3556 -> 86T3680
- R27, R30: MPN MCMR06X1201FTL -> CRCW0603374KFKEA.; OC_NEWARK 86T3525 -> 27W4235
- R43, R44, R45: MPN MCMR06X4701FTL -> MCMR06X2701FTL; OC_NEWARK 86T3649 -> 86T3598
- R65: MPN MCMR06X33R0FTL -> MCMR06X1000FTL; OC_NEWARK 86T3614 -> 86T3504
- T2: MPN (none) -> MMBT2222ALT3G; OC_NEWARK (none) -> 10N9478
- TP3, TP6: OC_NEWARK (none) -> unknown
- U3: MPN (none) -> AT24C512C-SSHM-B; OC_NEWARK (none) -> 68T4128
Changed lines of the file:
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@@
 </part>
 <part name="J6" library="con-molex" deviceset="22-?-03" device="05-7038">
-<attribute name="MPN" value="22-05-7028"/>
-<attribute name="OC_NEWARK" value="25M1728"/>
+<attribute name="MPN" value="22-05-7038"/>
+<attribute name="OC_NEWARK" value="26M6362"/>
 </part>
 <part name="P+12" library="supply1" deviceset="+5V" device=""/>
@@
 </part>
 <part name="J7" library="con-molex" deviceset="22-?-03" device="05-7038">
-<attribute name="MPN" value="22-05-7028"/>
-<attribute name="OC_NEWARK" value="25M1728"/>
+<attribute name="MPN" value="22-05-7038"/>
+<attribute name="OC_NEWARK" value="26M6362"/>
 </part>
 <part name="P+13" library="supply1" deviceset="+5V" device=""/>
@@
 <part name="U3" library="atmel" deviceset="AT24C512C-SSHM-B" device="">
 <attribute name="MF" value=""/>
+<attribute name="MPN" value="AT24C512C-SSHM-B"/>
+<attribute name="OC_NEWARK" value="68T4128"/>
 </part>
 <part name="+3V315" library="supply1" deviceset="+3V3" device=""/>
@@
 <part name="R11" library="rcl" deviceset="R-EU_" device="R0603" value="10K">
 <attribute name="MF" value=""/>
-<attribute name="MPN" value="MCMR06X4701FTL"/>
-<attribute name="OC_NEWARK" value="86T3649"/>
+<attribute name="MPN" value="MCMR06X1002FTL"/>
+<attribute name="OC_NEWARK" value="86T3506"/>
 </part>
 <part name="X3" library="crystal" deviceset="ASE" device="" value="ASE-12">
@@
 <part name="R43" library="rcl" deviceset="R-EU_" device="R0603" value="2K7">
 <attribute name="MF" value=""/>
-<attribute name="MPN" value="MCMR06X4701FTL"/>
-<attribute name="OC_NEWARK" value="86T3649"/>
+<attribute name="MPN" value="MCMR06X2701FTL"/>
+<attribute name="OC_NEWARK" value="86T3598"/>
 </part>
 <part name="R46" library="rcl" deviceset="R-EU_" device="R0603" value="1K">
@@
 <part name="R45" library="rcl" deviceset="R-EU_" device="R0603" value="2K7">
 <attribute name="MF" value=""/>
-<attribute name="MPN" value="MCMR06X4701FTL"/>
-<attribute name="OC_NEWARK" value="86T3649"/>
+<attribute name="MPN" value="MCMR06X2701FTL"/>
+<attribute name="OC_NEWARK" value="86T3598"/>
 </part>
 <part name="R47" library="rcl" deviceset="R-EU_" device="R0603" value="1K">
@@
 <part name="R44" library="rcl" deviceset="R-EU_" device="R0603" value="2K7">
 <attribute name="MF" value=""/>
-<attribute name="MPN" value="MCMR06X4701FTL"/>
-<attribute name="OC_NEWARK" value="86T3649"/>
+<attribute name="MPN" value="MCMR06X2701FTL"/>
+<attribute name="OC_NEWARK" value="86T3598"/>
 </part>
 <part name="J8" library="con-molex" deviceset="22-?-05" device="05-7058">
-<attribute name="MPN" value="22-05-7048"/>
-<attribute name="OC_NEWARK" value="26M6363"/>
+<attribute name="MF" value="MOLEX"/>
+<attribute name="MPN" value="22-05-7058"/>
+<attribute name="OC_NEWARK" value="55H9619"/>
 </part>
 <part name="P+9" library="supply1" deviceset="+5V" device=""/>
@@
 <part name="R25" library="rcl" deviceset="R-EU_" device="R0603" value="60.4">
 <attribute name="MF" value=""/>
-<attribute name="MPN" value="MCMR06X1801FTL"/>
-<attribute name="OC_NEWARK" value="86T3556"/>
+<attribute name="MPN" value="MCMR06X60R4FTL"/>
+<attribute name="OC_NEWARK" value="86T3680"/>
 </part>
 <part name="R26" library="rcl" deviceset="R-EU_" device="R0603" value="60.4">
 <attribute name="MF" value=""/>
-<attribute name="MPN" value="MCMR06X1801FTL"/>
-<attribute name="OC_NEWARK" value="86T3556"/>
+<attribute name="MPN" value="MCMR06X60R4FTL"/>
+<attribute name="OC_NEWARK" value="86T3680"/>
 </part>
 <part name="R27" library="rcl" deviceset="R-EU_" device="R0603" value="374K">
 <attribute name="MF" value=""/>
-<attribute name="MPN" value="MCMR06X1201FTL"/>
-<attribute name="OC_NEWARK" value="86T3525"/>
+<attribute name="MPN" value="CRCW0603374KFKEA."/>
+<attribute name="OC_NEWARK" value="27W4235"/>
 </part>
 <part name="R30" library="rcl" deviceset="R-EU_" device="R0603" value="374K">
 <attribute name="MF" value=""/>
-<attribute name="MPN" value="MCMR06X1201FTL"/>
-<attribute name="OC_NEWARK" value="86T3525"/>
+<attribute name="MPN" value="CRCW0603374KFKEA."/>
+<attribute name="OC_NEWARK" value="27W4235"/>
 </part>
 <part name="GND44" library="supply1" deviceset="GND" device=""/>
@@
 <attribute name="OC_NEWARK" value="15R2205"/>
 </part>
-<part name="J1" library="con-molex" deviceset="22-?-02" device="05-7028"/>
+<part name="J1" library="con-molex" deviceset="22-?-02" device="05-7028">
+<attribute name="MPN" value="22-05-7028"/>
+<attribute name="OC_NEWARK" value="25M1728"/>
+</part>
 <part name="GND1" library="supply1" deviceset="GND" device=""/>
 <part name="P+1" library="supply1" deviceset="+5V" device=""/>
-<part name="T2" library="transistor" deviceset="MMBT2222AL" device=""/>
+<part name="T2" library="transistor" deviceset="MMBT2222AL" device="">
+<attribute name="MF" value=""/>
+<attribute name="MPN" value="MMBT2222ALT3G"/>
+<attribute name="OC_NEWARK" value="10N9478"/>
+</part>
 <part name="R65" library="rcl" deviceset="R-EU_" device="R0603" value="100">
 <attribute name="MF" value=""/>
-<attribute name="MPN" value="MCMR06X33R0FTL"/>
-<attribute name="OC_NEWARK" value="86T3614"/>
+<attribute name="MPN" value="MCMR06X1000FTL"/>
+<attribute name="OC_NEWARK" value="86T3504"/>
 </part>
 <part name="P+25" library="supply1" deviceset="+5V" device=""/>
@@
 <attribute name="OC_NEWARK" value="86T3504"/>
 </part>
-<part name="TP3" library="testpad" deviceset="TP" device="B1,27"/>
-<part name="TP6" library="testpad" deviceset="TP" device="B1,27"/>
+<part name="TP3" library="testpad" deviceset="TP" device="B1,27">
+<attribute name="MF" value=""/>
+<attribute name="MPN" value=""/>
+<attribute name="OC_NEWARK" value="unknown"/>
+</part>
+<part name="TP6" library="testpad" deviceset="TP" device="B1,27">
+<attribute name="MF" value=""/>
+<attribute name="MPN" value=""/>
+<attribute name="OC_NEWARK" value="unknown"/>
+</part>
 <part name="R81" library="rcl" deviceset="R-EU_" device="R0603" value="1K5">
 <attribute name="MF" value=""/>
@@
 </instance>
 <instance part="+3V322" gate="G$1" x="358.14" y="66.04"/>
-<instance part="TP3" gate="G$1" x="17.78" y="22.86" rot="R90"/>
-<instance part="TP6" gate="G$1" x="17.78" y="12.7" rot="R90"/>
+<instance part="TP3" gate="G$1" x="17.78" y="22.86" rot="R90">
+<attribute name="OC_NEWARK" x="17.78" y="22.86" size="1.778" layer="96" display="off"/>
+<attribute name="MF" x="17.78" y="22.86" size="1.778" layer="96" display="off"/>
+<attribute name="MPN" x="17.78" y="22.86" size="1.778" layer="96" display="off"/>
+</instance>
+<instance part="TP6" gate="G$1" x="17.78" y="12.7" rot="R90">
+<attribute name="OC_NEWARK" x="17.78" y="12.7" size="1.778" layer="96" display="off"/>
+<attribute name="MF" x="17.78" y="12.7" size="1.778" layer="96" display="off"/>
+<attribute name="MPN" x="17.78" y="12.7" size="1.778" layer="96" display="off"/>
+</instance>
 </instances>
 <busses>
@@
 <attribute name="MPN" x="40.64" y="73.66" size="1.778" layer="96" display="off"/>
 </instance>
-<instance part="T2" gate="1" x="332.74" y="215.9" rot="MR0"/>
+<instance part="T2" gate="1" x="332.74" y="215.9" rot="MR0">
+<attribute name="OC_NEWARK" x="332.74" y="215.9" size="1.778" layer="96" display="off"/>
+<attribute name="MF" x="332.74" y="215.9" size="1.778" layer="96" display="off"/>
+<attribute name="MPN" x="332.74" y="215.9" size="1.778" layer="96" display="off"/>
+</instance>
 <instance part="R65" gate="G$1" x="330.2" y="233.68" rot="MR270">
 <attribute name="OC_NEWARK" x="330.2" y="233.68" size="1.778" layer="96" display="off"/>

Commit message: Generate BOM
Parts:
- C52, C53: MPN (none) -> MC0805X226M6R3CT; OC_NEWARK unknown -> 33R0743
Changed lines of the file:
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@@
 <part name="C53" library="rcl" deviceset="C-EU" device="C0805" value="22uF">
 <attribute name="MF" value=""/>
-<attribute name="MPN" value=""/>
-<attribute name="OC_NEWARK" value="unknown"/>
+<attribute name="MPN" value="MC0805X226M6R3CT"/>
+<attribute name="OC_NEWARK" value="33R0743"/>
 </part>
 <part name="C52" library="rcl" deviceset="C-EU" device="C0805" value="22uF">
 <attribute name="MF" value=""/>
-<attribute name="MPN" value=""/>
-<attribute name="OC_NEWARK" value="unknown"/>
+<attribute name="MPN" value="MC0805X226M6R3CT"/>
+<attribute name="OC_NEWARK" value="33R0743"/>
 </part>
 <part name="U4" library="NXP" deviceset="LPC1768FBD100" device="">
